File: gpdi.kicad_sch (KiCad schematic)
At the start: 21 parts, among them U1 LFE5U-85F-6BG381C, U11 PCA9306D

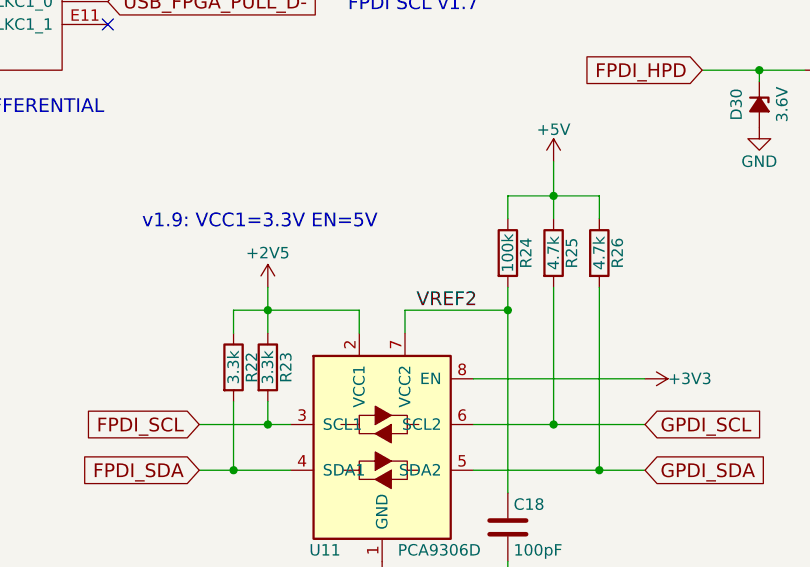
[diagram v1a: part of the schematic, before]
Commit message: add pwr_flag to VREF2
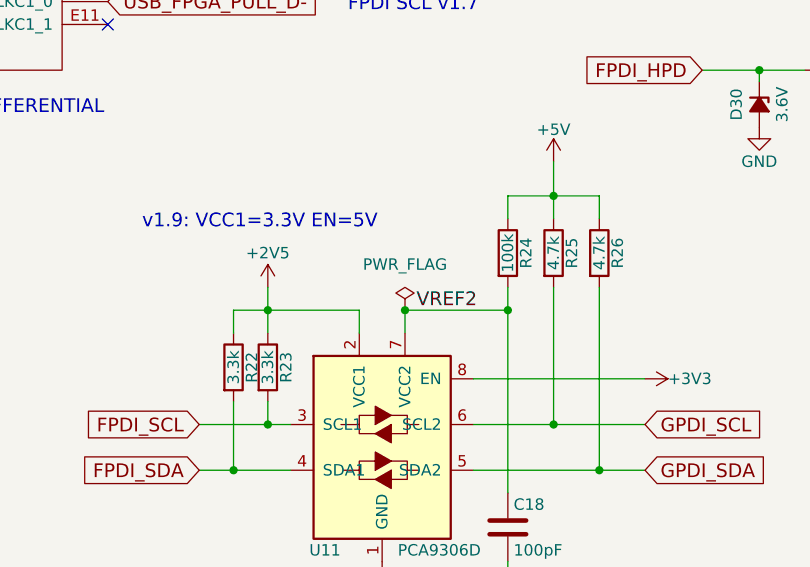
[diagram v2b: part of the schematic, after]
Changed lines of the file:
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@@
 	)
 	(junction
+		(at 143.51 125.73)
+		(diameter 0)
+		(color 0 0 0 0)
+	)
+	(junction
 		(at 128.27 125.73)
 		(diameter 0)
@@
 					(unit 1)
 				)
+			)
+		)
+	)
+	(symbol
+		(lib_id "power:PWR_FLAG")
+		(at 143.51 125.73 0)
+		(unit 1)
+		(exclude_from_sim no)
+		(in_bom yes)
+		(on_board yes)
+		(dnp no)
+		(fields_autoplaced yes)
+		(property "Reference" "#FLG06"
+			(at 143.51 123.825 0)
+			(effects
+				(font
+					(size 1.27 1.27)
+				)
+				(hide yes)
+			)
+		)
+		(property "Value" "PWR_FLAG"
+			(at 143.51 120.65 0)
+			(effects
+				(font
+					(size 1.27 1.27)
+				)
+			)
+		)
+		(property "Footprint" ""
+			(at 143.51 125.73 0)
+			(effects
+				(font
+					(size 1.27 1.27)
+				)
+				(hide yes)
+			)
+		)
+		(property "Datasheet" "~"
+			(at 143.51 125.73 0)
+			(effects
+				(font
+					(size 1.27 1.27)
+				)
+				(hide yes)
+			)
+		)
+		(property "Description" "Special symbol for telling ERC where power comes from"
+			(at 143.51 125.73 0)
+			(effects
+				(font
+					(size 1.27 1.27)
+				)
+				(hide yes)
+			)
+		)
+		(pin "1"
+		)
+		(instances
+			(project "ulx3s"
+				(path "/49a43414-f3c1-43b2-ad20-ac3166075f21/00000000-0000-0000-0000-000058d686d9"
+					(reference "#FLG06")
+					(unit 1)
+				)
